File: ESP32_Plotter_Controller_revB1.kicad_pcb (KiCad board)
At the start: 2 copper layers, 99.1 x 55.4 mm, 57 parts, among them J1 ARM JTAG 10pin, J10 Pen Lift, J11 Vselect, J12 X Motor, J13 Y Motor, J14 Neo Pixel LEDs, J15 Pen Direction, J16 Aux Port (I2C), J17 USB_C_Receptacle_USB2.0, J18 E-Stop, J19 Y Limit Switch, J2 Power (12v), J3 5V Aux, J4 Vin Aux, J5 X Limit Switch, J6 Aux Port (SPI), J7 X Limit, J8 Micro_SD_Card_TF-01A, J9 Y Limit, SW1 RESET, SW2 BOOT, U1 ESP32-WROOM-32D, U2 TMC2130, U3 TMC2130, U4 XL1509, U5 CH340C, U6 AMS1117-3.3

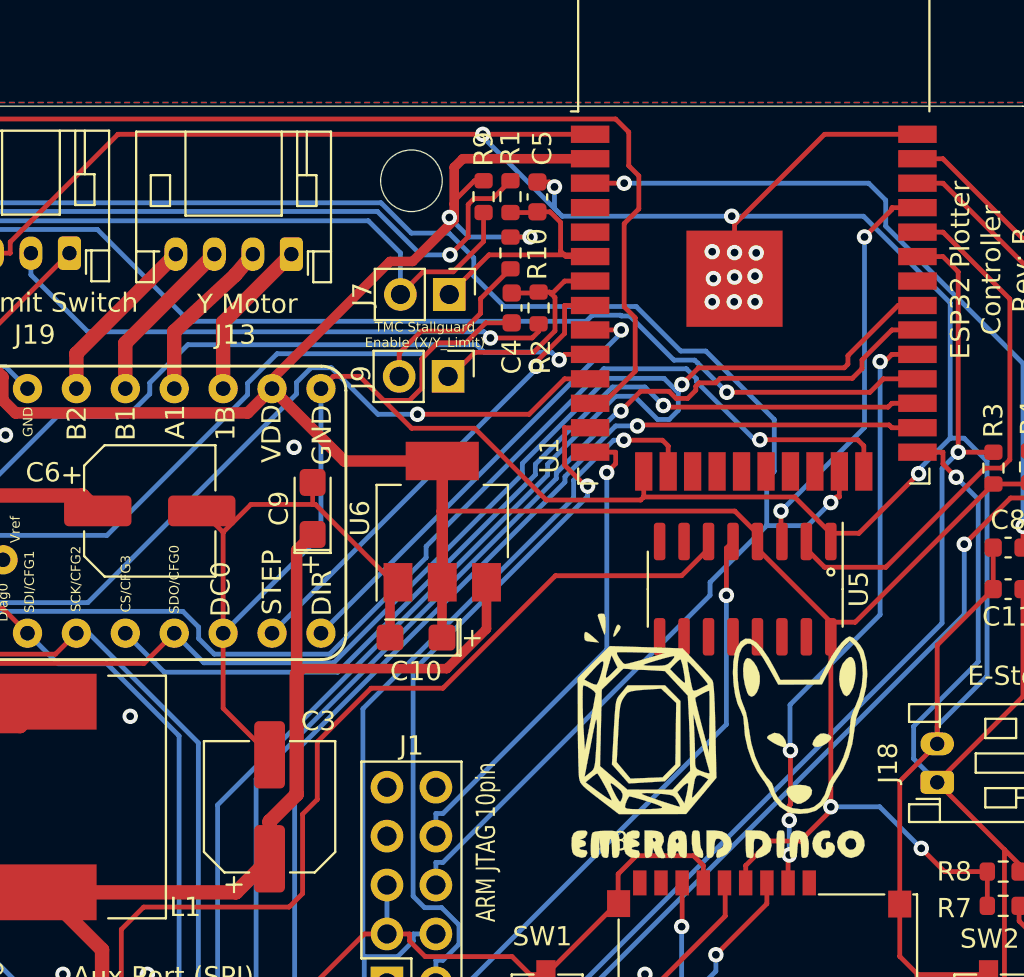
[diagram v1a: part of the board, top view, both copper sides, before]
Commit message: Add decoupling capacitors
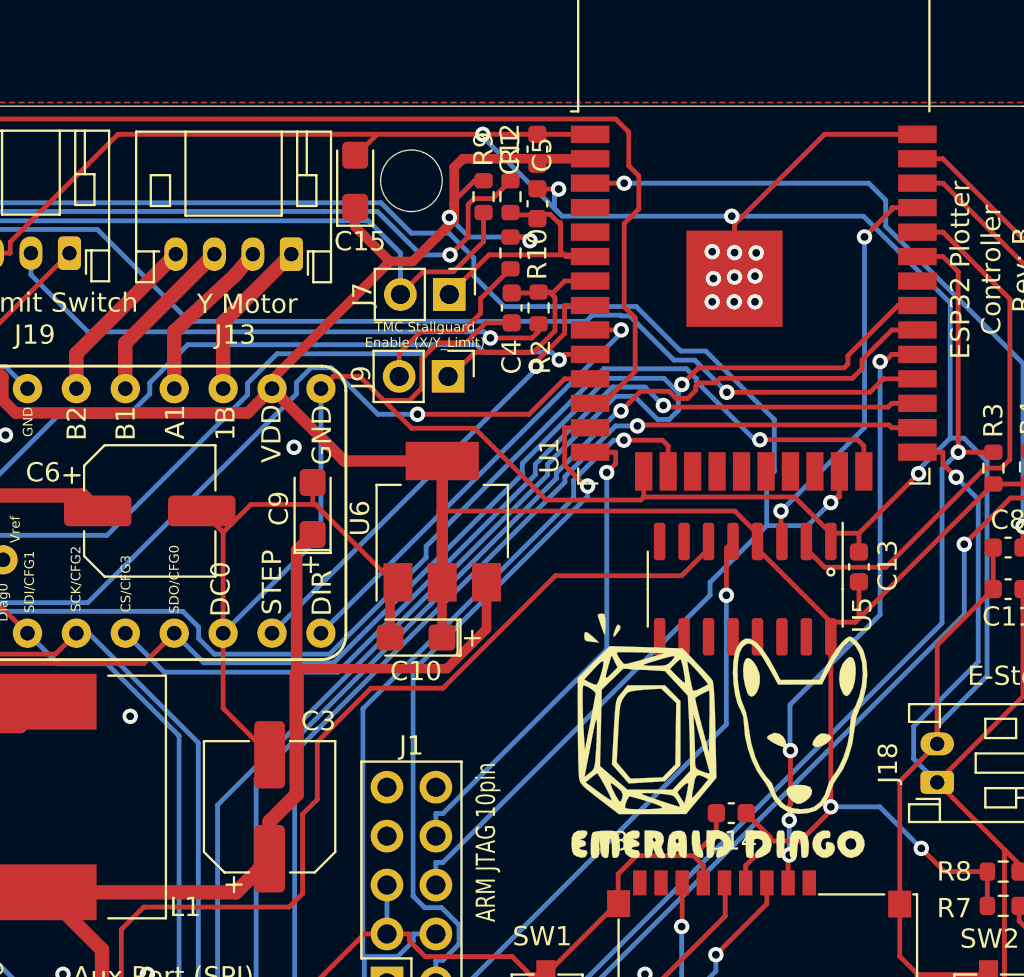
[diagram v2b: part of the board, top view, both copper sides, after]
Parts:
- added C12: 100nF, Capacitor_SMD:C_0603_1608Metric, F.Cu at (96.7, 71.3)
- added C13: 100nF, Capacitor_SMD:C_0603_1608Metric, F.Cu at (113.4, 93.0)
- added C14: 100nF, Capacitor_SMD:C_0603_1608Metric, F.Cu at (106.8, 105.7)
- added C15: 22uF 10v, Capacitor_Tantalum_SMD:CP_EIA-3216-18_Kemet-A, F.Cu at (87.2, 72.9)
- C11, C8: value 0.1uF -> 100nF
- R10, R3, R4, R9: value 10K -> 10k
- moved C5 0.35 mm to (96.7, 74.1)
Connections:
- R7 pad 1: +3V3 -> /EN
- R7 pad 2: /EN -> +3V3
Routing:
- net +3V3: track 216.2 -> 224.4 mm
- net GND: track 514.7 -> 520.7 mm

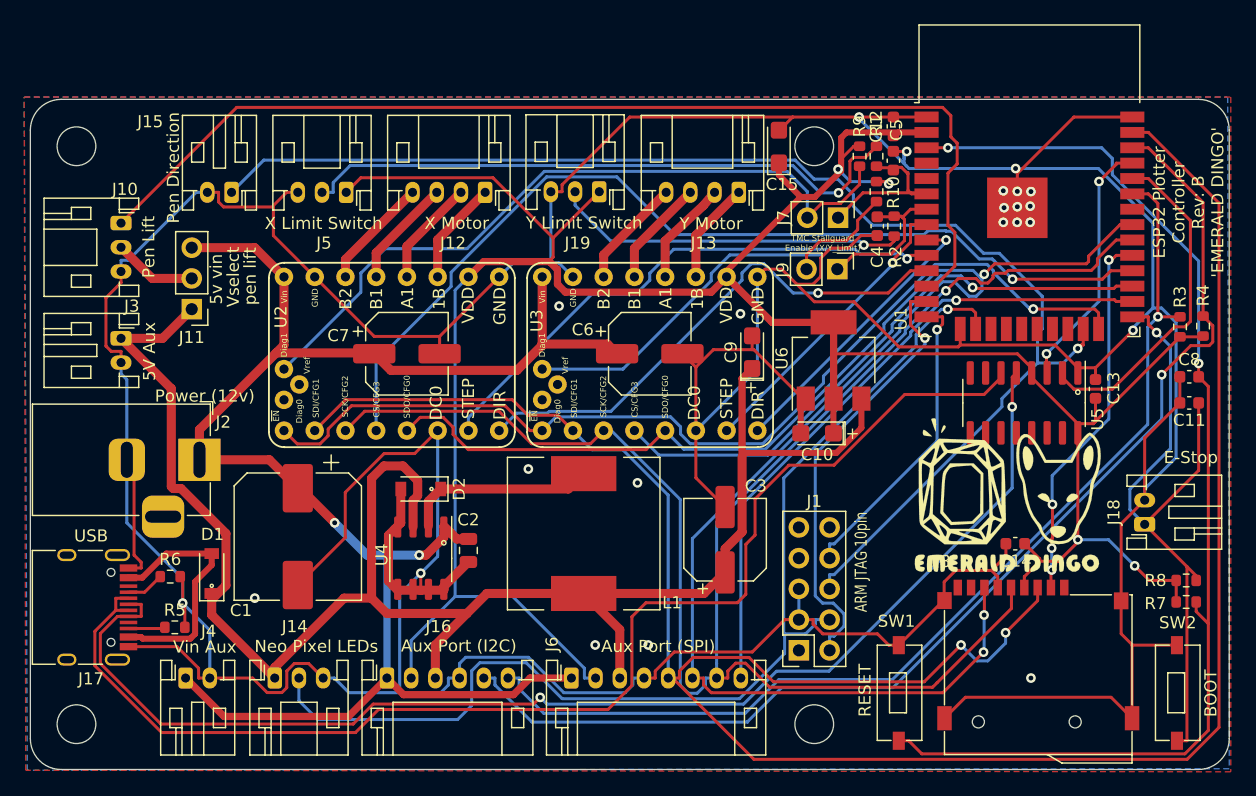
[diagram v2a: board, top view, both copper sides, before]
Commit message: Fix USB differential pair routing
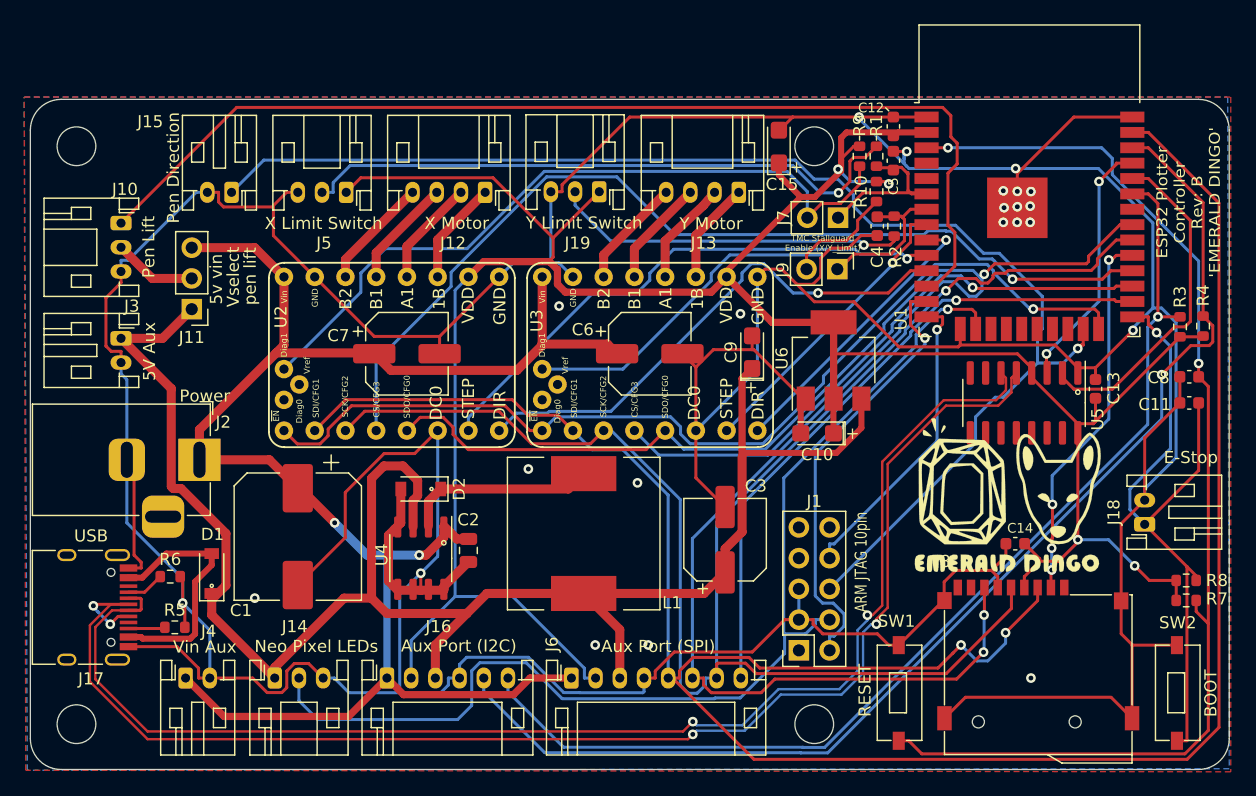
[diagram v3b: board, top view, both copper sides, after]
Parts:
- J2: value Power (12v) -> Power
- moved R7 0.13 mm to (120.9, 110.4), turned to 180 degrees
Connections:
- net Net-(J17-PadA6) renamed /D+
- net Net-(J17-PadA7) renamed /D-
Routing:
- net /D+: track 104.1 -> 116.3 mm, vias 2 -> 4
- net /D-: track 105.6 -> 110.4 mm, vias 0 -> 2
- net /SDA: track 87.4 -> 89.8 mm
- net /SCL: track 96.8 -> 99.2 mm
- net /MOSI: track 188.4 -> 187.5 mm
- net /SCK: track 140.1 -> 139.5 mm
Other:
- board text added: "+"

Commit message: Tweaked some ground planes and silkscreen
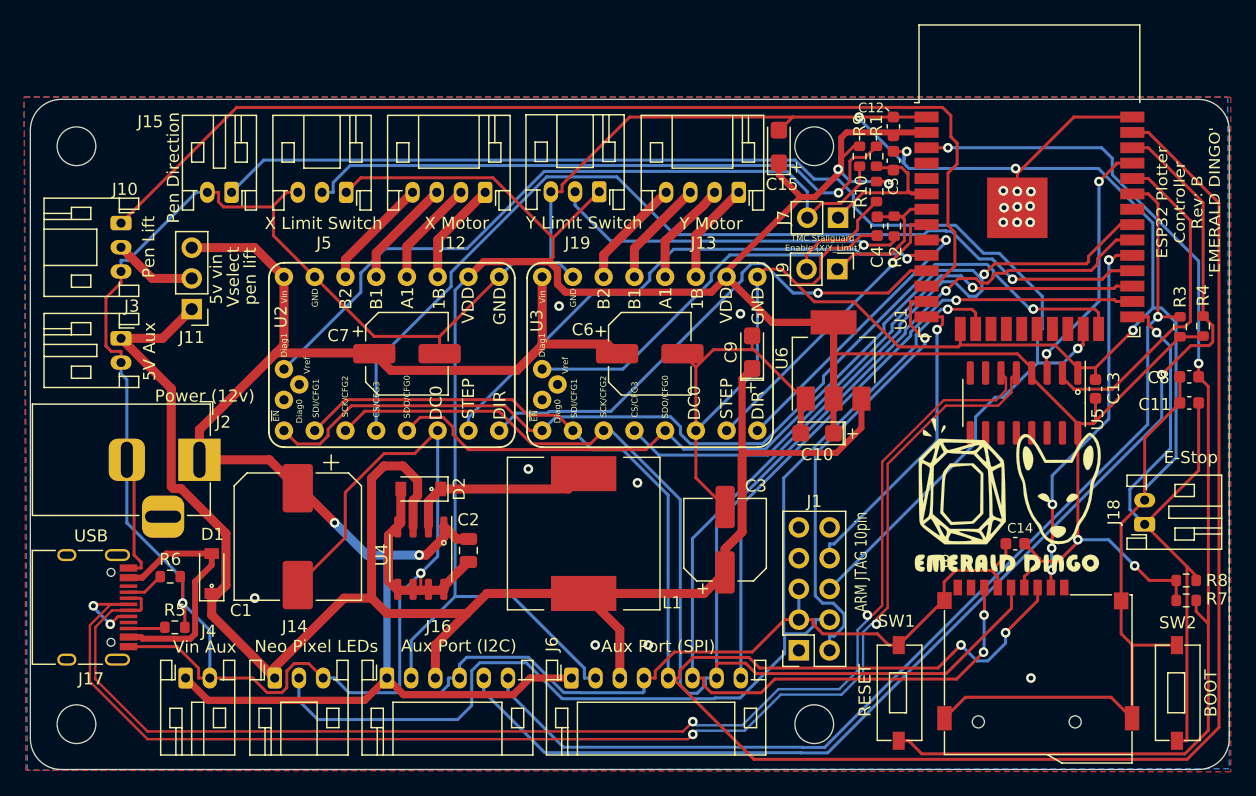
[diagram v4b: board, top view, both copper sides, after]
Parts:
- J2: value Power -> Power (12v)
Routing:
- net /Vin: track 136.1 -> 135.0 mm

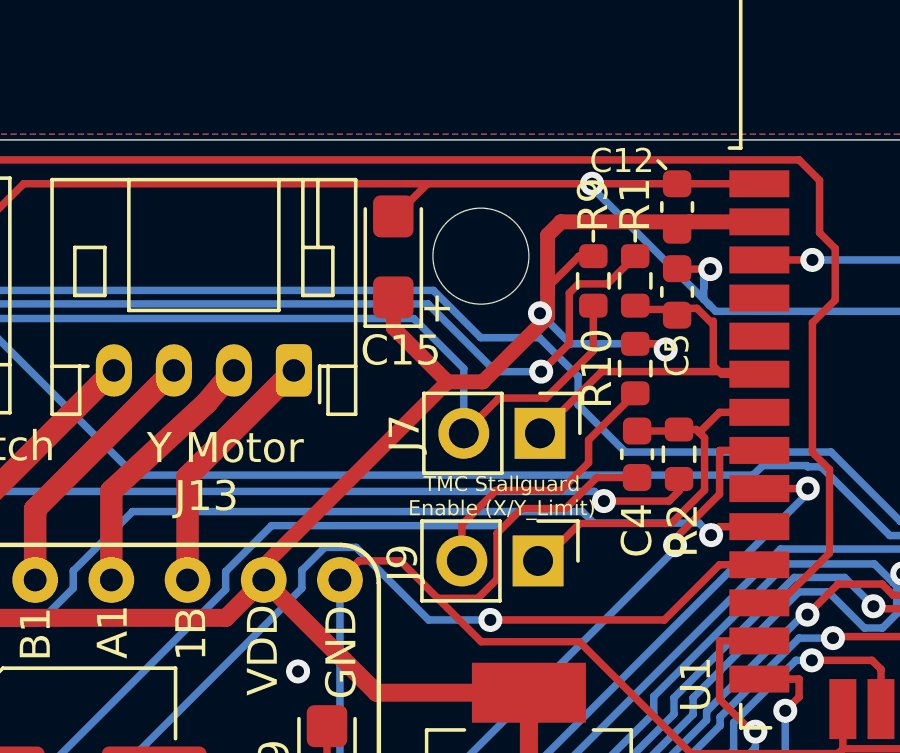
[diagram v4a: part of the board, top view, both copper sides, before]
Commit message: Fix screw head clearance problem with C15
Decoupling cap for ESP32 would be in the way of an M3 screw head. Moved down to nearer J17. Clearance checked in CAD.
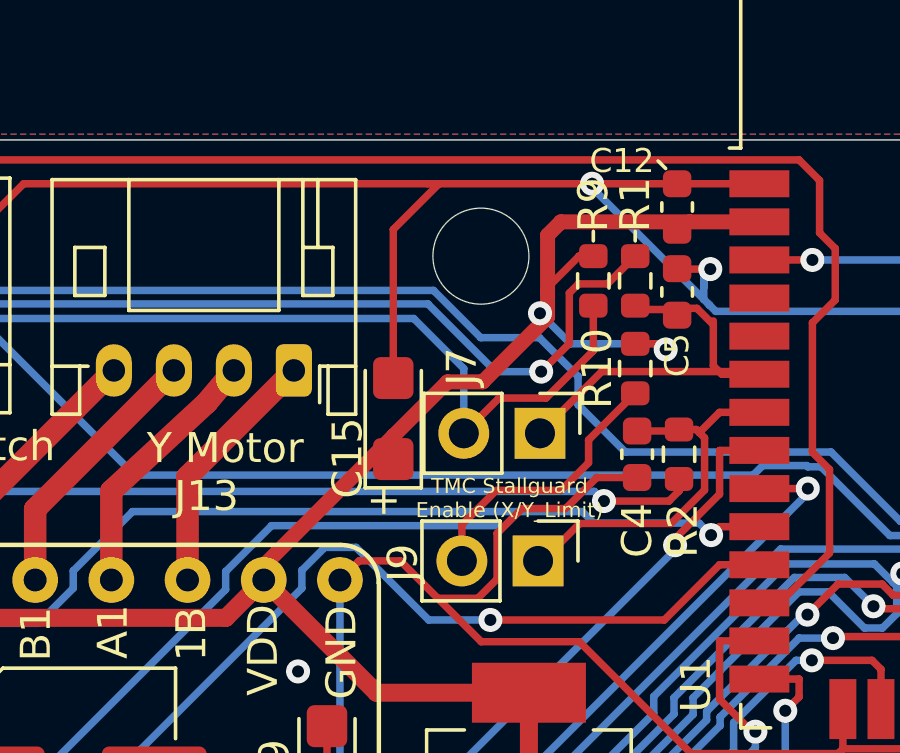
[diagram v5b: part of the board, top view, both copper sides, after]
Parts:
- moved C15 5.39 mm to (87.2, 78.3)
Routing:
- net GND: track 520.9 -> 526.4 mm
- net +3V3: track 224.4 -> 221.7 mm
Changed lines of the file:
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@@
     (thickness 1.6)
     (drawings 19)
-    (tracks 980)
+    (tracks 982)
     (zones 0)
     (modules 61)
@@
   )
   (setup
-    (last_trace_width 0.6)
+    (last_trace_width 0.25)
     (user_trace_width 0.5)
     (user_trace_width 0.6)
@@
     (descr "Through hole straight pin header, 1x02, 2.54mm pitch, single row")
     (tags "Through hole pin header THT 1x02 2.54mm single row")
-    (fp_text reference J7 (at 0 4.5085 90) (layer F.SilkS)
+    (fp_text reference J7 (at -2.2225 2.6035 90) (layer F.SilkS)
       (effects (font (size 1 1) (thickness 0.15)))
     )
@@
   )
   (module Capacitor_Tantalum_SMD:CP_EIA-3216-18_Kemet-A (layer F.Cu)
-    (at 87.249 72.9234 90)
+    (at 87.249 78.312 90)
     (descr "Tantalum Capacitor SMD Kemet-A (3216-18 Metric), IPC_7351 nominal, (Body size from: http://www.kemet.com/Lists/ProductCatalog/Attachments/253/KEM_TC101_STD.pdf), generated with kicad-footprint-generator")
     (tags "capacitor tantalum")
     (attr smd)
-    (fp_text reference C15 (at -3.1242 0.254 180) (layer F.SilkS)
+    (fp_text reference C15 (at -1.317 -1.524 270) (layer F.SilkS)
       (effects (font (size 1 1) (thickness 0.15)))
     )
@@
     )
   )
-  (gr_text + (at 88.7095 74.6125) (layer F.SilkS)
+  (gr_text + (at 86.9315 81.026) (layer F.SilkS)
     (effects (font (size 1 1) (thickness 0.15)))
   )
@@
     (effects (font (size 1 1) (thickness 0.15)))
   )
-  (gr_text "TMC Stallguard\nEnable (X/Y_Limit)" (at 90.8685 80.899) (layer F.SilkS)
+  (gr_text "TMC Stallguard\nEnable (X/Y_Limit)" (at 91.1225 80.9625) (layer F.SilkS)
     (effects (font (size 0.5 0.5) (thickness 0.1)))
   )
@@
   (segment (start 106.0066 106.7614) (end 104.818 107.95) (width 0.25) (layer F.Cu) (net 1))
   (segment (start 106.0066 105.7402) (end 106.0066 106.7614) (width 0.25) (layer F.Cu) (net 1))
-  (segment (start 87.3036 71.5734) (end 88.392 70.485) (width 0.25) (layer F.Cu) (net 1))
-  (segment (start 87.249 71.5734) (end 87.3036 71.5734) (width 0.25) (layer F.Cu) (net 1))
-  (segment (start 88.392 70.485) (end 93.8764 70.485) (width 0.25) (layer F.Cu) (net 1))
   (segment (start 74.928 70.485) (end 88.392 70.485) (width 0.25) (layer F.Cu) (net 1))
   (segment (start 76.0151 118.0539) (end 70.804813 118.0539) (width 0.25) (layer B.Cu) (net 1))
@@
   (segment (start 66.5552 115.124) (end 61.455 115.124) (width 0.25) (layer B.Cu) (net 1))
   (segment (start 76.104 116.84) (end 76.104 117.965) (width 0.25) (layer B.Cu) (net 1))
+  (segment (start 87.249 76.962) (end 87.249 72.009) (width 0.25) (layer F.Cu) (net 1))
+  (segment (start 87.249 72.009) (end 88.773 70.485) (width 0.25) (layer F.Cu) (net 1))
+  (segment (start 88.773 70.485) (end 93.8764 70.485) (width 0.25) (layer F.Cu) (net 1))
+  (segment (start 88.392 70.485) (end 88.773 70.485) (width 0.25) (layer F.Cu) (net 1))
   (segment (start 85.0392 91.266) (end 84.209 92.0962) (width 0.6) (layer F.Cu) (net 2))
   (segment (start 61.468 111.506) (end 54.864 111.506) (width 0.75) (layer F.Cu) (net 2))
@@
   (segment (start 82.931 83.215) (end 82.931 83.693) (width 0.5) (layer F.Cu) (net 16))
   (segment (start 92.837 71.755) (end 92.3925 72.1995) (width 0.5) (layer F.Cu) (net 16))
-  (segment (start 89.057 77.089) (end 82.931 83.215) (width 0.5) (layer F.Cu) (net 16))
   (segment (start 92.3925 73.947) (end 92.3925 74.1045) (width 0.25) (layer F.Cu) (net 16))
   (segment (start 93.9165 72.898) (end 93.4415 72.898) (width 0.25) (layer F.Cu) (net 16))
@@
   (segment (start 97.1296 71.755) (end 92.828 71.755) (width 0.5) (layer F.Cu) (net 16))
   (segment (start 99.441 71.755) (end 97.1296 71.755) (width 0.5) (layer F.Cu) (net 16))
-  (segment (start 87.249 75.281) (end 89.057 77.089) (width 0.5) (layer F.Cu) (net 16))
-  (segment (start 87.249 74.2734) (end 87.249 75.281) (width 0.5) (layer F.Cu) (net 16))
+  (segment (start 87.249 78.897) (end 87.264 78.882) (width 0.25) (layer F.Cu) (net 16))
+  (segment (start 87.249 79.662) (end 87.249 78.897) (width 0.25) (layer F.Cu) (net 16))
+  (segment (start 87.264 78.882) (end 82.931 83.215) (width 0.5) (layer F.Cu) (net 16))
+  (segment (start 89.057 77.089) (end 87.264 78.882) (width 0.5) (layer F.Cu) (net 16))
   (segment (start 52.705 84.963) (end 46.355 91.313) (width 0.25) (layer B.Cu) (net 17))
   (segment (start 52.705 83.382) (end 52.705 84.963) (width 0.25) (layer B.Cu) (net 17))

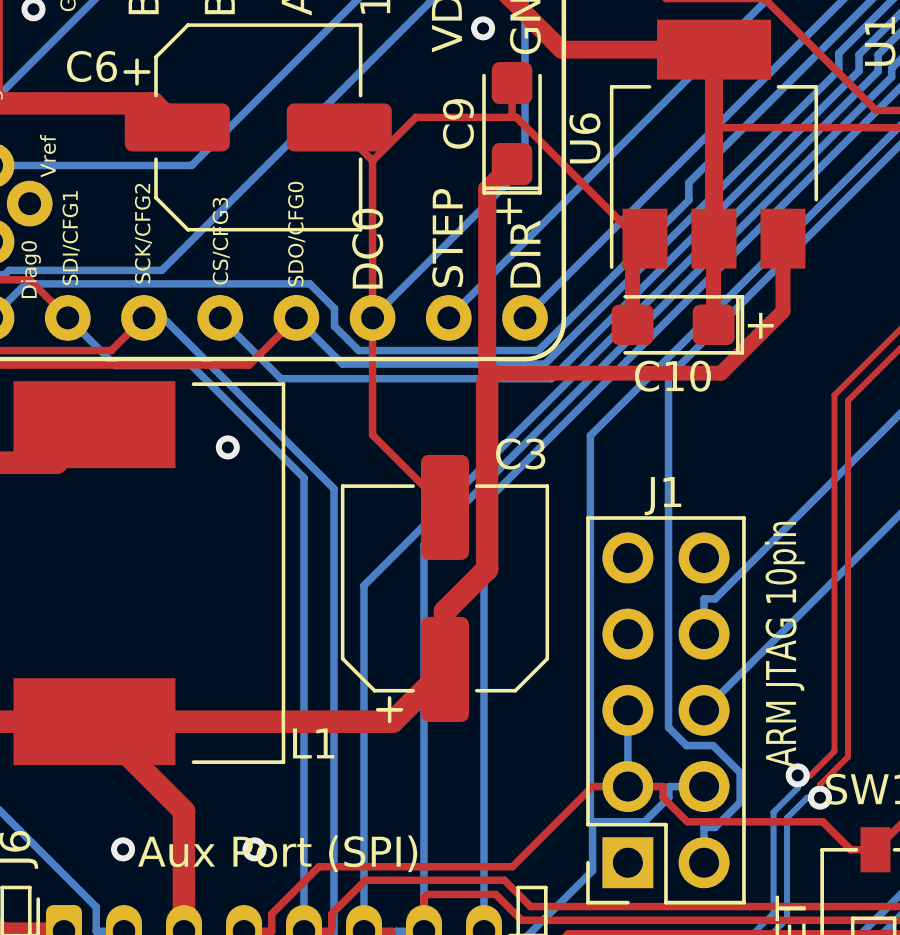
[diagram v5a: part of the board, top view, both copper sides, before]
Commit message: Update LCSC part numbers and production files
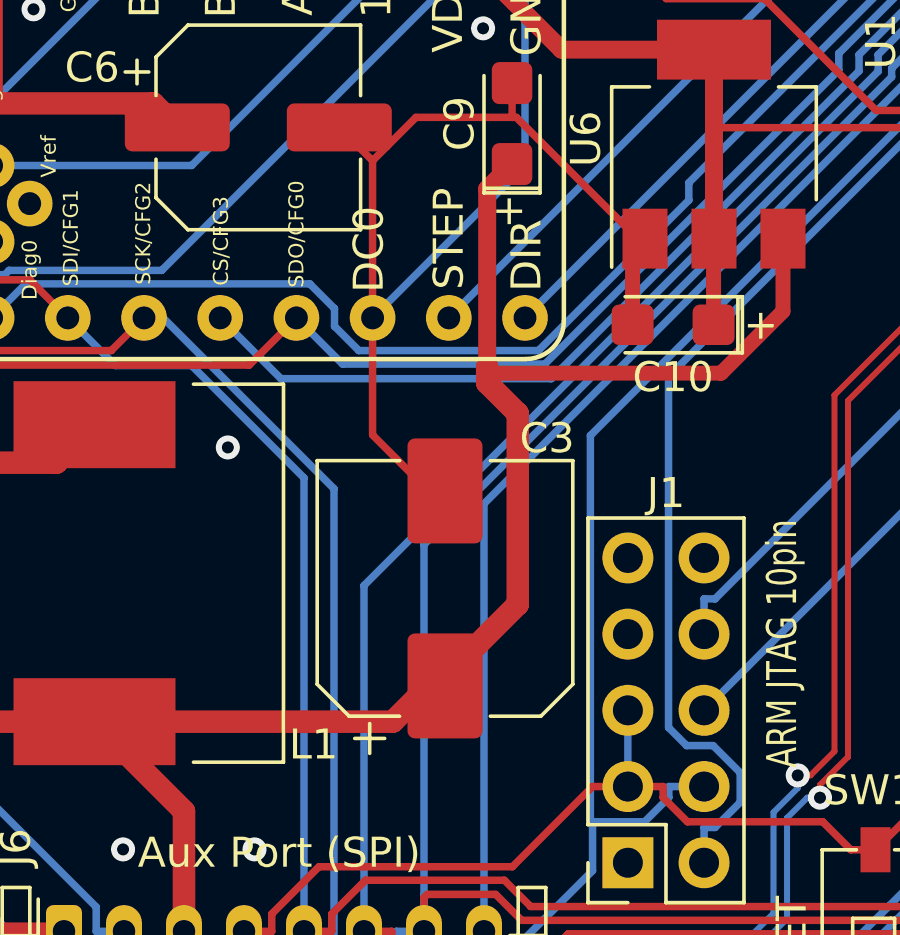
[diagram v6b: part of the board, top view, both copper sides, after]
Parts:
- C3: footprint Capacitor_SMD:CP_Elec_6.3x7.7 -> Capacitor_SMD:CP_Elec_8x10
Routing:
- net +5V: track 148.7 -> 150.1 mm
